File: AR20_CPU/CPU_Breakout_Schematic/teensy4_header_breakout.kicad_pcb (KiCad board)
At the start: 2 copper layers, 12 parts, among them SW1 SW_SPST, U2 MCP2551-I-SN

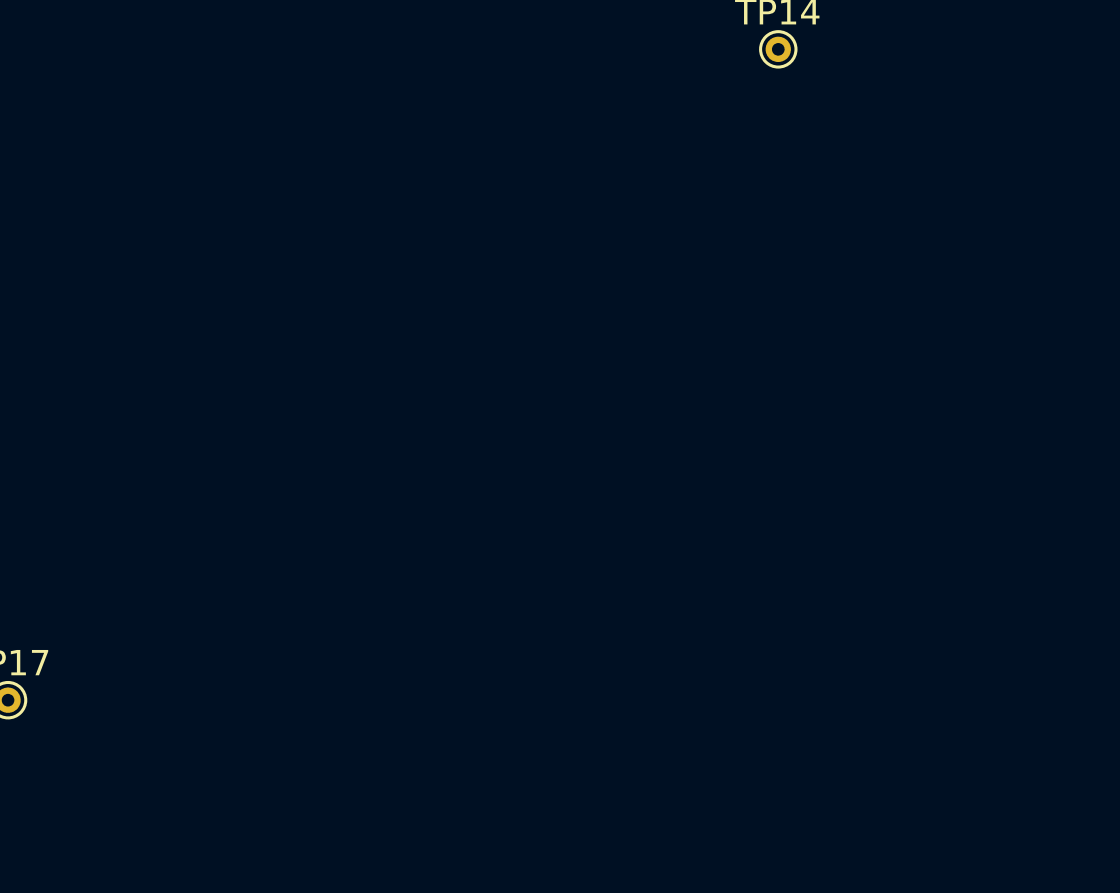
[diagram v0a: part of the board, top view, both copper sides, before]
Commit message: Added footprint to connectors
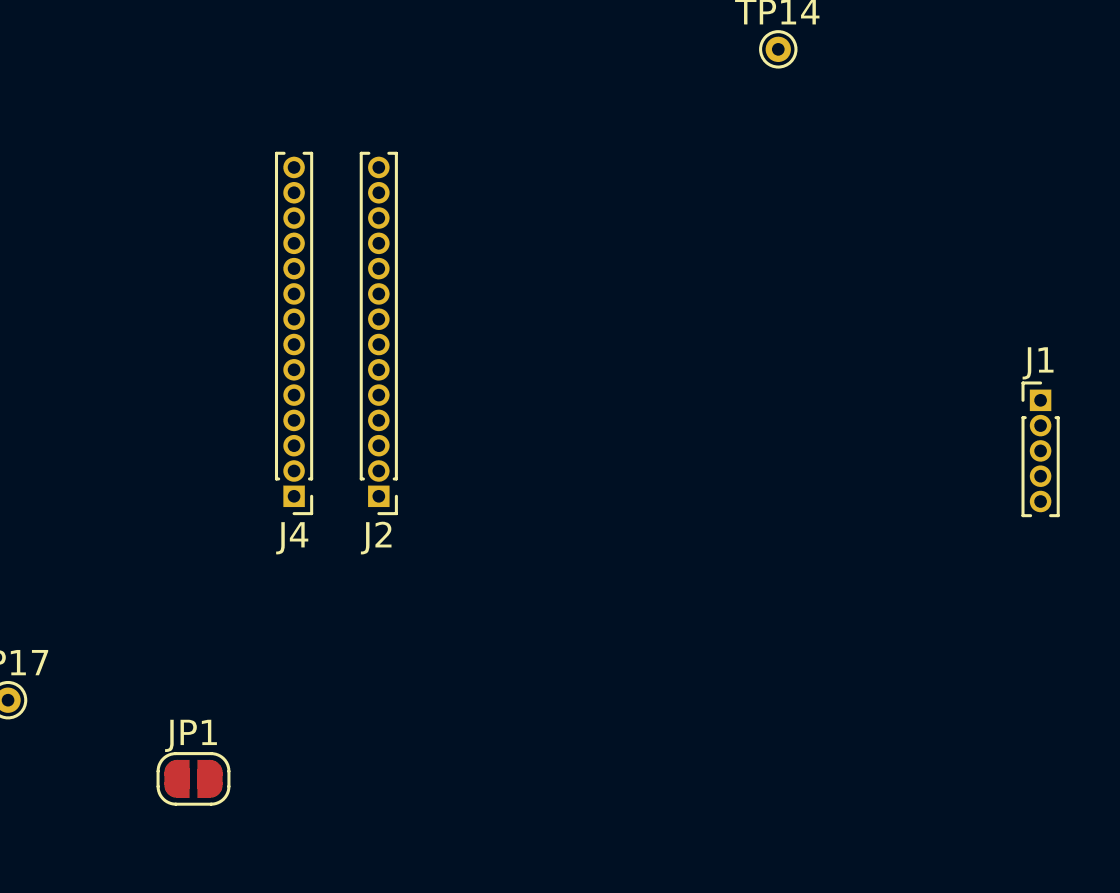
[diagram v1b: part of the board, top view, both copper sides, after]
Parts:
- added J1: Conn_01x05, Connector_PinHeader_1.00mm:PinHeader_1x05_P1.00mm_Vertical, F.Cu at (180.7, 109.7)
- added J2: Conn_01x14, Connector_PinHeader_1.00mm:PinHeader_1x14_P1.00mm_Vertical, F.Cu at (154.6, 113.5)
- added J4: Conn_01x14, Connector_PinHeader_1.00mm:PinHeader_1x14_P1.00mm_Vertical, F.Cu at (151.2, 113.5)
- added JP1: SolderJumper_2_Open, Jumper:SolderJumper-2_P1.3mm_Open_RoundedPad1.0x1.5mm, F.Cu at (147.2, 124.7)
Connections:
- R2 pad 2: (no net) -> Net-(JP1-Pad1)
- TP12 pad 1: (no net) -> CS_SD
- TP13 pad 1: (no net) -> MOSI_SD
- TP14 pad 1: (no net) -> MISO_SD
- U2 pad 6: (no net) -> Net-(H2-Pad1)

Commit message: Edited test points
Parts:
- added TP10: TestPoint, TestPoint:TestPoint_THTPad_D1.0mm_Drill0.5mm, F.Cu at (193.6, 92.7)
- added TP11: TestPoint, TestPoint:TestPoint_THTPad_D1.0mm_Drill0.5mm, F.Cu at (199.7, 95.8)
- added TP16: TestPoint, TestPoint:TestPoint_THTPad_D1.0mm_Drill0.5mm, F.Cu at (196.7, 92.7)
- added TP18: TestPoint, TestPoint:TestPoint_THTPad_D1.0mm_Drill0.5mm, F.Cu at (193.6, 89.7)
- added TP2: TestPoint, TestPoint:TestPoint_THTPad_D1.0mm_Drill0.5mm, F.Cu at (162.6, 113.5)
- added TP20: TestPoint, TestPoint:TestPoint_THTPad_D1.0mm_Drill0.5mm, F.Cu at (199.7, 92.7)
- added TP21: TestPoint, TestPoint:TestPoint_THTPad_D1.0mm_Drill0.5mm, F.Cu at (196.7, 89.7)
- added TP22: TestPoint, TestPoint:TestPoint_THTPad_D1.0mm_Drill0.5mm, F.Cu at (199.7, 89.7)
- added TP3: TestPoint, TestPoint:TestPoint_THTPad_D1.0mm_Drill0.5mm, F.Cu at (162.6, 112.3)
- added TP4: TestPoint, TestPoint:TestPoint_THTPad_D1.0mm_Drill0.5mm, F.Cu at (162.7, 111.3)
- added TP5: TestPoint, TestPoint:TestPoint_THTPad_D1.0mm_Drill0.5mm, F.Cu at (162.9, 110.0)
- added TP6: TestPoint, TestPoint:TestPoint_THTPad_D1.0mm_Drill0.5mm, F.Cu at (162.9, 109.2)
- added TP7: TestPoint, TestPoint:TestPoint_THTPad_D1.0mm_Drill0.5mm, F.Cu at (162.9, 108.1)
- added TP8: TestPoint, TestPoint:TestPoint_THTPad_D1.0mm_Drill0.5mm, F.Cu at (162.9, 107.1)
- added TP9: TestPoint, TestPoint:TestPoint_THTPad_D1.0mm_Drill0.5mm, F.Cu at (196.7, 95.8)
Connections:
- BT1 pad 1: VBAT -> (no net)
- BT1 pad 2: GND_BATT -> (no net)
- J2 pad 1: (no net) -> Net-(J2-Pad1)
- J2 pad 10: (no net) -> Net-(J2-Pad10)
- J2 pad 11: CS_SD -> (no net)
- J2 pad 12: MOSI_SD -> (no net)
- J2 pad 13: MISO_SD -> (no net)
- J2 pad 2: (no net) -> Net-(J2-Pad2)
- J2 pad 3: (no net) -> Net-(J2-Pad3)
- J2 pad 4: (no net) -> Net-(J2-Pad4)
- J2 pad 5: (no net) -> Net-(J2-Pad5)
- J2 pad 6: (no net) -> Net-(J2-Pad6)
- J2 pad 7: (no net) -> Net-(J2-Pad7)
- J2 pad 8: (no net) -> Net-(J2-Pad8)
- J2 pad 9: (no net) -> Net-(J2-Pad9)
- TP12 pad 1: CS_SD -> Net-(J2-Pad8)
- TP13 pad 1: MOSI_SD -> Net-(J2-Pad9)
- TP14 pad 1: MISO_SD -> Net-(J2-Pad10)
- TP15 pad 1: VBAT -> (no net)
- TP17 pad 1: GND_BATT -> (no net)

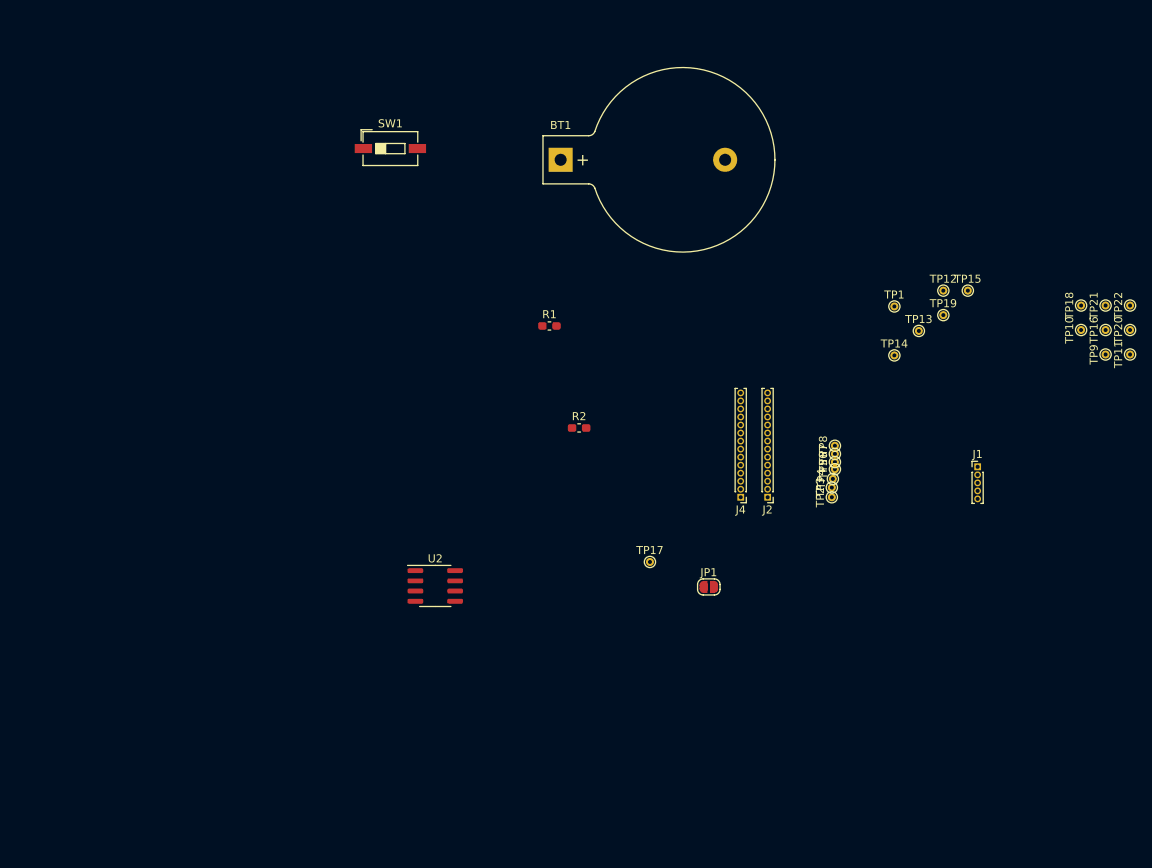
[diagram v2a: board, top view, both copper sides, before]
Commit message: ADDED NEW FOOTPRINT TO TEENSY CONNECTORS
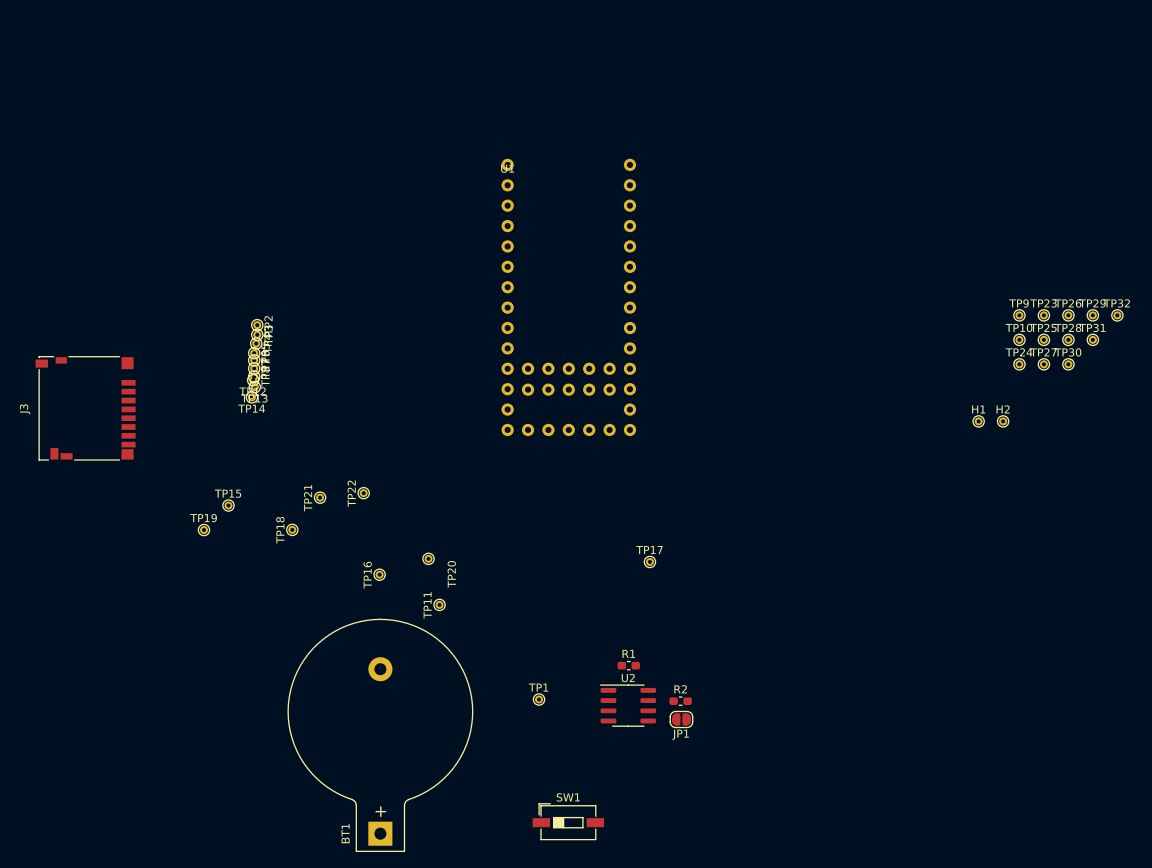
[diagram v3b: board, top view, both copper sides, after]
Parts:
- removed J1: Conn_01x05, Connector_PinHeader_1.00mm:PinHeader_1x05_P1.00mm_Vertical
- removed J2, J4: Conn_01x14, Connector_PinHeader_1.00mm:PinHeader_1x14_P1.00mm_Vertical
- added H1: CANH_out, TestPoint:TestPoint_THTPad_D1.0mm_Drill0.5mm, F.Cu at (180.8, 104.1)
- added H2: CANL_out, TestPoint:TestPoint_THTPad_D1.0mm_Drill0.5mm, F.Cu at (183.9, 104.1)
- added J3: Micro_SD_Card, Connector_Card:microSD_HC_Hirose_DM3D-SF, F.Cu at (69.6, 102.5)
- added TP23: TestPoint, TestPoint:TestPoint_THTPad_D1.0mm_Drill0.5mm, F.Cu at (189.0, 90.9)
- added TP24: TestPoint, TestPoint:TestPoint_THTPad_D1.0mm_Drill0.5mm, F.Cu at (185.9, 97.0)
- added TP25: TestPoint, TestPoint:TestPoint_THTPad_D1.0mm_Drill0.5mm, F.Cu at (189.0, 93.9)
- added TP26: TestPoint, TestPoint:TestPoint_THTPad_D1.0mm_Drill0.5mm, F.Cu at (192.0, 90.9)
- added TP27: TestPoint, TestPoint:TestPoint_THTPad_D1.0mm_Drill0.5mm, F.Cu at (189.0, 97.0)
- added TP28: TestPoint, TestPoint:TestPoint_THTPad_D1.0mm_Drill0.5mm, F.Cu at (192.0, 93.9)
- added TP29: TestPoint, TestPoint:TestPoint_THTPad_D1.0mm_Drill0.5mm, F.Cu at (195.1, 90.9)
- added TP30: TestPoint, TestPoint:TestPoint_THTPad_D1.0mm_Drill0.5mm, F.Cu at (192.0, 97.0)
- added TP31: TestPoint, TestPoint:TestPoint_THTPad_D1.0mm_Drill0.5mm, F.Cu at (195.1, 93.9)
- added TP32: TestPoint, TestPoint:TestPoint_THTPad_D1.0mm_Drill0.5mm, F.Cu at (198.1, 90.9)
- added U1: Teensy_pins, Teensy_Footprint_Library:Teensy_40_footprint, F.Cu at (122.2, 72.1)
- moved TP18 102.2 mm to (95.4, 117.6)
- moved TP21 100.7 mm to (98.8, 113.6)
- moved TP22 98.3 mm to (104.2, 113.0)
- moved TP15 95.9 mm to (87.4, 114.6)
- moved TP19 95.9 mm to (84.4, 117.6)
- moved TP16 95.4 mm to (106.2, 123.2)
- moved TP20 91.9 mm to (112.3, 121.2)
- moved TP11 91.5 mm to (113.7, 126.9)
- moved BT1 86.9 mm to (106.3, 155.4), turned to 90 degrees
- moved SW1 86.9 mm to (129.7, 154.1)
- moved TP12 86.7 mm to (90.5, 99.0), turned to 180 degrees
- moved TP13 83.0 mm to (90.7, 99.8), turned to 180 degrees
- moved TP14 80.2 mm to (90.3, 101.1), turned to 180 degrees
- moved TP2 74.7 mm to (91.0, 92.1), turned to 270 degrees
- moved TP3 74.1 mm to (91.0, 93.3), turned to 270 degrees
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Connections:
- BT1 pad 1: (no net) -> VBAT
- BT1 pad 2: (no net) -> GND_BATT
- SW1 pad 2: (no net) -> ON_OFF
- TP1 pad 1: Ground -> Net-(TP1-Pad1)
- TP10 pad 1: (no net) -> Net-(TP10-Pad1)
- TP11 pad 1: (no net) -> 3.3V
- TP15 pad 1: (no net) -> Net-(TP15-Pad1)
- TP16 pad 1: (no net) -> Net-(TP16-Pad1)
- TP17 pad 1: (no net) -> Net-(TP17-Pad1)
- TP18 pad 1: (no net) -> Net-(TP18-Pad1)
- TP19 pad 1: (no net) -> Net-(TP19-Pad1)
- TP20 pad 1: (no net) -> Net-(TP20-Pad1)
- TP21 pad 1: (no net) -> Net-(TP21-Pad1)
- TP22 pad 1: (no net) -> Net-(TP22-Pad1)
- TP9 pad 1: (no net) -> Net-(TP9-Pad1)
- U2 pad 1: (no net) -> 22_CTX1
- U2 pad 3: (no net) -> Vinn_5V
- U2 pad 4: (no net) -> 23_CRX1

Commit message: FOOTPRINT IS DONE
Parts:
- removed TP1, TP10, TP11, TP12, TP13, TP14, TP15, TP16, TP17, TP18, TP19, TP2, TP20, TP21, TP22, TP23, TP24, TP25, TP26, TP27, TP28, TP29, TP3, TP30, TP31, TP32, TP4, TP5, TP6, TP7, TP8, TP9: TestPoint, TestPoint:TestPoint_THTPad_D1.0mm_Drill0.5mm
- added J1: Conn_2Rows-34Pins, Teensy_Footprint_Library:PINS_IO_TEENSY, F.Cu at (125.5, 117.8)
- moved J3 58.0 mm to (121.8, 127.7), turned to 180 degrees
- moved H2 57.7 mm to (151.3, 56.4), turned to 270 degrees
- moved JP1 56.1 mm to (137.1, 85.5)
- moved R2 54.4 mm to (132.0, 85.9)
- moved H1 54.2 mm to (131.3, 82.2), turned to 270 degrees
- moved U2 48.9 mm to (134.4, 90.7), turned to 180 degrees
- moved R1 40.1 mm to (134.7, 94.5), turned to 180 degrees
- moved BT1 38.2 mm to (132.5, 127.6), turned to 0 degrees
- moved SW1 33.5 mm to (107.0, 129.5), turned to 90 degrees
- moved U1 4.88 mm to (127.1, 72.1)
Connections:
- net CS_SD renamed 10_CS
- net MISO_SD renamed 12_MISO
- net MOSI_SD renamed 11_MOSI
- net SCK_SD renamed 13(LED)
- J3 pad 4: 3.3V -> 3V3
- U1 pad 1: Net-(TP1-Pad1) -> Ground
- U1 pad 11: Net-(TP6-Pad1) -> 4_BCLK2
- U1 pad 12: Net-(TP15-Pad1) -> 21_A7
- U1 pad 13: Net-(TP7-Pad1) -> 5_IN2
- U1 pad 14: Net-(TP16-Pad1) -> 20_A6
- U1 pad 15: Net-(TP8-Pad1) -> 6_OUT1D
- U1 pad 16: Net-(TP17-Pad1) -> 19_A5
- U1 pad 17: Net-(TP12-Pad1) -> 7_RX2_OUT1A
- U1 pad 18: Net-(TP18-Pad1) -> 18_A4
- U1 pad 19: Net-(TP13-Pad1) -> 8_IN1
- U1 pad 20: Net-(TP19-Pad1) -> 17_A3
- U1 pad 21: Net-(TP14-Pad1) -> 9_OUT1C
- U1 pad 22: Net-(TP20-Pad1) -> 16_A2
- U1 pad 24: Net-(TP21-Pad1) -> 15_A1
- U1 pad 26: Net-(TP22-Pad1) -> 14_A0
- U1 pad 3: Net-(TP2-Pad1) -> 0_RX1
- U1 pad 30: Net-(TP26-Pad1) -> 3V3
- U1 pad 32: Net-(TP27-Pad1) -> PROGRAMM
- U1 pad 34: Net-(TP28-Pad1) -> 24_A10
- U1 pad 35: Net-(TP9-Pad1) -> 25_A11
- U1 pad 36: Net-(TP29-Pad1) -> 26_A12
- U1 pad 37: Net-(TP10-Pad1) -> 27_A13
- U1 pad 38: Net-(TP30-Pad1) -> 28_RX7
- U1 pad 39: Net-(TP23-Pad1) -> 29_TX7
- U1 pad 4: (no net) -> GND_1
- U1 pad 40: Net-(TP31-Pad1) -> 30_CRX3
- U1 pad 41: Net-(TP24-Pad1) -> 31_CTX3
- U1 pad 42: Net-(TP32-Pad1) -> 32_OUT1B
- U1 pad 43: Net-(TP25-Pad1) -> 33_MCLK2
- U1 pad 5: Net-(TP3-Pad1) -> 1_TX1
- U1 pad 7: Net-(TP4-Pad1) -> 2_OUT2
- U1 pad 9: Net-(TP5-Pad1) -> 3_LRCLK2

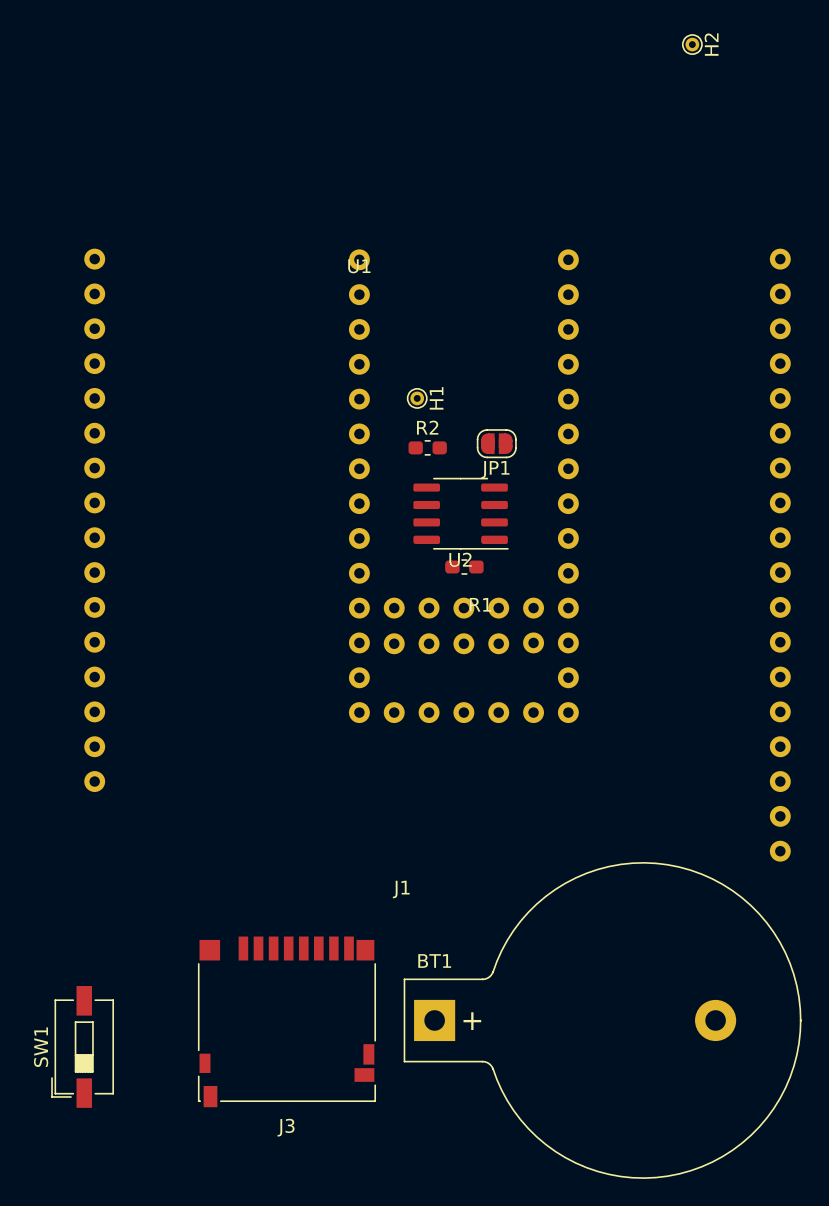
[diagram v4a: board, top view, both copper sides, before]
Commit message: Added some trace to PCB
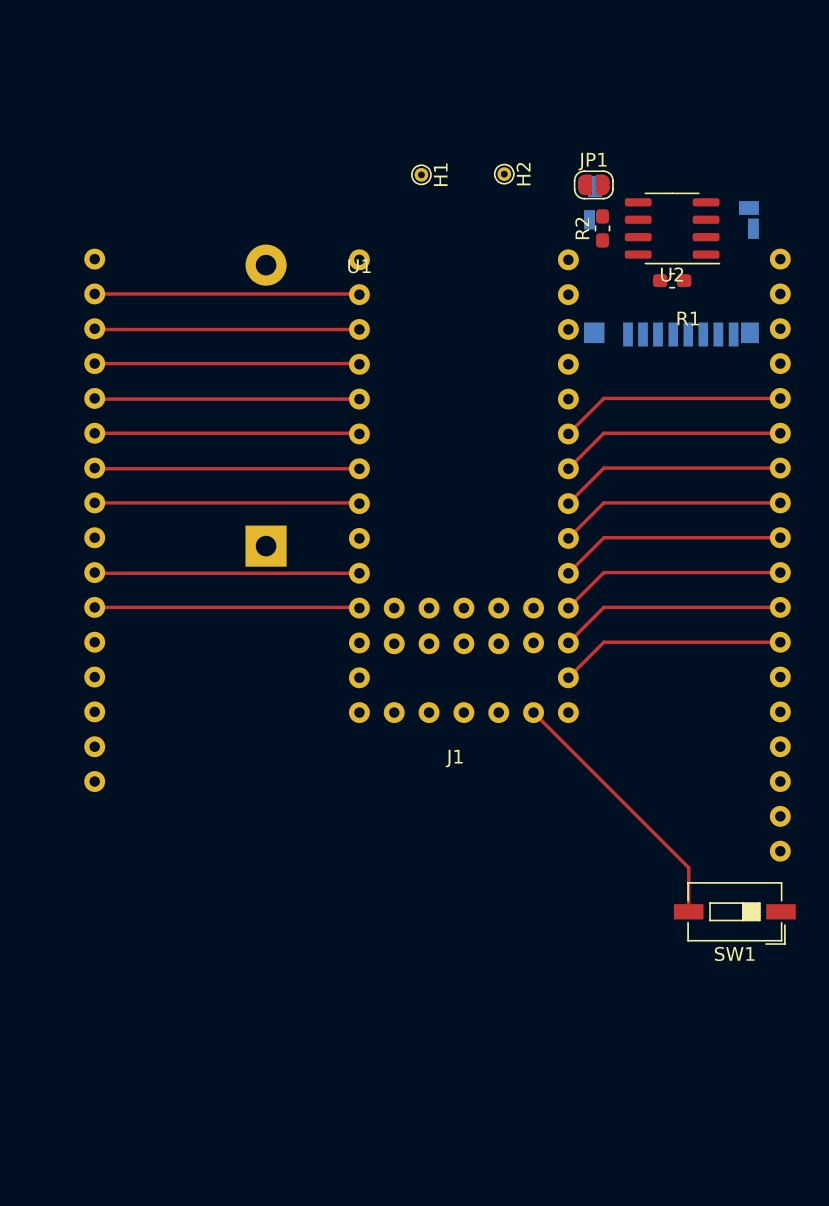
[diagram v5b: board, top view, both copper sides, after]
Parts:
- BT1, J3: moved to B.Cu
- moved J3 62.2 mm to (149.8, 72.2)
- moved SW1 48.5 mm to (154.4, 119.7), turned to 180 degrees
- moved BT1 36.7 mm to (120.2, 93.0), turned to 90 degrees
- moved U2 25.9 mm to (149.9, 69.8)
- moved R1 25.8 mm to (149.9, 73.7)
- moved R2 20.5 mm to (144.8, 69.8), turned to 90 degrees
- moved JP1 20.2 mm to (144.1, 66.7), turned to 0 degrees
- moved H2 16.7 mm to (137.6, 65.9)
- moved H1 16.3 mm to (131.6, 65.9)
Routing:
- net 5_IN2: track 0.00 -> 19.3 mm
- net 3_LRCLK2: track 0.00 -> 19.3 mm
- net 9_OUT1C: track 0.00 -> 19.3 mm
- net 6_OUT1D: track 0.00 -> 19.3 mm
- net 4_BCLK2: track 0.00 -> 19.3 mm
- net 2_OUT2: track 0.00 -> 19.3 mm
- net 0_RX1: track 0.00 -> 19.3 mm
- net 8_IN1: track 0.00 -> 19.3 mm
- net 1_TX1: track 0.00 -> 19.3 mm
- net ON_OFF: track 0.00 -> 19.2 mm
- net 21_A7: track 0.00 -> 16.5 mm
- net 20_A6: track 0.00 -> 16.5 mm
- net 19_A5: track 0.00 -> 16.5 mm
- net 18_A4: track 0.00 -> 16.5 mm
- net 17_A3: track 0.00 -> 16.5 mm
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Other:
- copper layers 2 -> 4

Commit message: initial traces is done
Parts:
- BT1: footprint Battery:BatteryHolder_Keystone_103_1x20mm -> Battery:BatteryHolder_Keystone_3034_1x20mm
- H1, H2: footprint TestPoint:TestPoint_THTPad_D1.0mm_Drill0.5mm -> TestPoint:TestPoint_THTPad_D1.5mm_Drill0.7mm
- moved J3 57.9 mm to (114.6, 118.1)
- moved BT1 29.0 mm to (136.4, 117.1), turned to 180 degrees
- moved H1 4.79 mm to (132.3, 61.2)
- moved H2 4.68 mm to (137.4, 61.2)
- moved U1 2.08 mm to (125.0, 72.1)
- moved J1 0.56 mm to (125.0, 117.9)
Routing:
- net 11_MOSI: track 0.00 -> 46.7 mm, vias 0 -> 2
- net 30_CRX3: track 0.00 -> 44.7 mm, vias 0 -> 2
- net 32_OUT1B: track 0.00 -> 44.3 mm, vias 0 -> 2
- net 27_A13: track 0.00 -> 40.6 mm
- net 13(LED): track 0.00 -> 40.3 mm
- net VBAT: track 0.00 -> 38.9 mm, vias 0 -> 2
- net 33_MCLK2: track 0.00 -> 34.3 mm, vias 0 -> 2
- net 24_A10: track 0.00 -> 31.8 mm, vias 0 -> 1
- net 31_CTX3: track 0.00 -> 31.5 mm
- net 10_CS: track 0.00 -> 30.8 mm, vias 0 -> 1
- net 3V3: track 0.00 -> 29.4 mm
- net 26_A12: track 0.00 -> 28.9 mm, vias 0 -> 1
- net Vinn_5V: track 0.00 -> 25.2 mm
- net 28_RX7: track 0.00 -> 24.7 mm
- net 25_A11: track 0.00 -> 23.8 mm
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- added copper zone on B.Cu, net Ground
- added copper zone on F.Cu, net Ground
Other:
- rule trace_min: 0.2 -> 0.007
